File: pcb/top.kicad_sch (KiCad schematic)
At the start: 76 parts, among them J1 Conn_01x01, J10 Conn_01x01, J11 Conn_01x01, J2 Conn_01x01, J3 Conn_01x06, J4 Conn_01x01, J5 Conn_01x01, J6 Conn_01x01, J7 Conn_01x01, J8 Conn_01x01, J9 Conn_01x01, Q1 2N7002, Q2 2N7002, Q3 2N7002, Q4 2N7002, U1 L78L05_SOT89, U2 PIC12F629-ISN, U3 L78L08_SO8

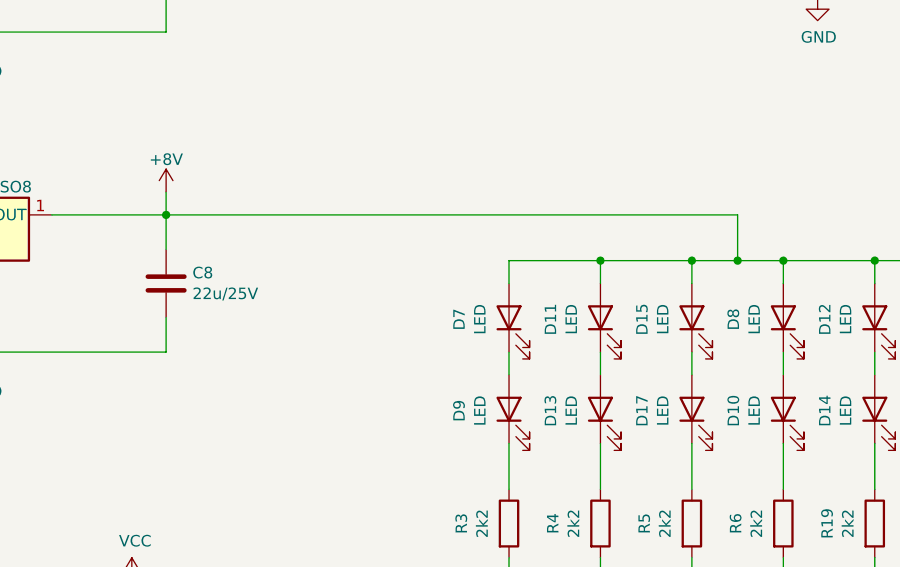
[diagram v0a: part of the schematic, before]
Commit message: Add optinal tantalum capacitor.
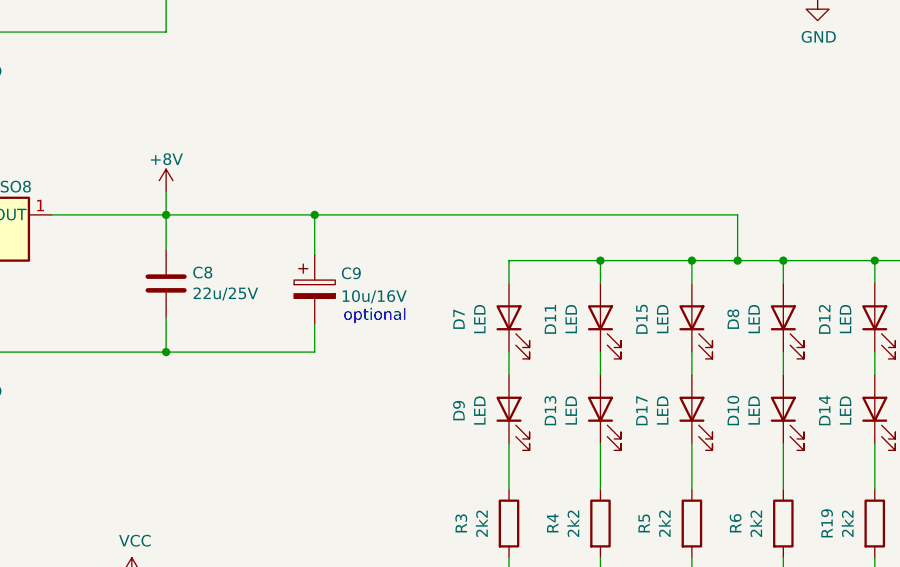
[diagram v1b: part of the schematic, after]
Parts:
- added C9: 10u/16V, Capacitor_Tantalum_SMD:CP_EIA-3216-10_Kemet-I, symbol Device:C_Polarized
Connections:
- net +8V: now also C9.1
- net GND: now also C9.2
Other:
- note added: "optional"
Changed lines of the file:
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@@
   (title_block
     (title "Osvětlení vozů Balm MTB model - horní deska")
-    (date "2021-12-23")
-    (rev "2.0")
+    (date "2023-03-18")
+    (rev "2.1")
     (company "Model Railroader Club Brno I – KMŽ Brno I – https://kmz-brno.cz/")
     (comment 1 "Jan Horáček; inspirováno https://usuaris.tinet.cat/fmco/dccfunc_en.html")
@@
   (junction (at 115.57 52.07) (diameter 0) (color 0 0 0 0)
   )
+  (junction (at 156.21 87.63) (diameter 0) (color 0 0 0 0)
+  )
   (junction (at 234.95 116.84) (diameter 0) (color 0 0 0 0)
   )
@@
   )
   (junction (at 83.82 44.45) (diameter 0) (color 0 0 0 0)
+  )
+  (junction (at 172.72 72.39) (diameter 0) (color 0 0 0 0)
   )
   (junction (at 92.71 36.83) (diameter 0) (color 0 0 0 0)
@@
     (stroke (width 0) (type default) (color 0 0 0 0))
   )
-  (wire (pts (xy 156.21 72.39) (xy 219.71 72.39))
+  (wire (pts (xy 172.72 72.39) (xy 219.71 72.39))
+    (stroke (width 0) (type default) (color 0 0 0 0))
+  )
+  (wire (pts (xy 156.21 72.39) (xy 172.72 72.39))
     (stroke (width 0) (type default) (color 0 0 0 0))
   )
@@
     (stroke (width 0) (type default) (color 0 0 0 0))
   )
+  (wire (pts (xy 172.72 84.455) (xy 172.72 87.63))
+    (stroke (width 0) (type default) (color 0 0 0 0))
+  )
   (wire (pts (xy 135.89 87.63) (xy 156.21 87.63))
     (stroke (width 0) (type default) (color 0 0 0 0))
@@
     (stroke (width 0) (type default) (color 0 0 0 0))
   )
+  (wire (pts (xy 172.72 87.63) (xy 156.21 87.63))
+    (stroke (width 0) (type default) (color 0 0 0 0))
+  )
   (wire (pts (xy 100.33 146.05) (xy 100.33 148.59))
     (stroke (width 0) (type default) (color 0 0 0 0))
@@
   )
   (wire (pts (xy 95.25 118.11) (xy 100.33 118.11))
+    (stroke (width 0) (type default) (color 0 0 0 0))
+  )
+  (wire (pts (xy 172.72 72.39) (xy 172.72 76.835))
     (stroke (width 0) (type default) (color 0 0 0 0))
   )
@@
   )
   (text "Programming\nconnector" (at 233.68 29.21 0)
+    (effects (font (size 1.27 1.27)) (justify left bottom))
+  )
+  (text "optional" (at 175.895 84.455 0)
     (effects (font (size 1.27 1.27)) (justify left bottom))
   )
@@
     (pin "1")
   )
+  (symbol (lib_id "Device:C_Polarized") (at 172.72 80.645 0) (unit 1)
+    (in_bom yes) (on_board yes) (fields_autoplaced)
+    (property "Reference" "C9" (id 0) (at 175.641 78.9213 0)
+      (effects (font (size 1.27 1.27)) (justify left))
+    )
+    (property "Value" "10u/16V" (id 1) (at 175.641 81.4582 0)
+      (effects (font (size 1.27 1.27)) (justify left))
+    )
+    (property "Footprint" "Capacitor_Tantalum_SMD:CP_EIA-3216-10_Kemet-I" (id 2) (at 173.6852 84.455 0)
+      (effects (font (size 1.27 1.27)) hide)
+    )
+    (property "Datasheet" "~" (id 3) (at 172.72 80.645 0)
+      (effects (font (size 1.27 1.27)) hide)
+    )
+    (pin "1")
+    (pin "2")
+  )
   (symbol (lib_id "Mechanical:MountingHole") (at 76.2 181.61 0) (unit 1)
     (in_bom yes) (on_board yes)
@@
       (reference "C8") (unit 1) (value "22u/25V") (footprint "Capacitor_SMD:C_0805_2012Metric_Pad1.18x1.45mm_HandSolder")
     )
+    (path "/802d2433-37f7-42c0-af96-9720c4dded53"
+      (reference "C9") (unit 1) (value "10u/16V") (footprint "Capacitor_Tantalum_SMD:CP_EIA-3216-10_Kemet-I")
+    )
     (path "/00000000-0000-0000-0000-000061c6e829"

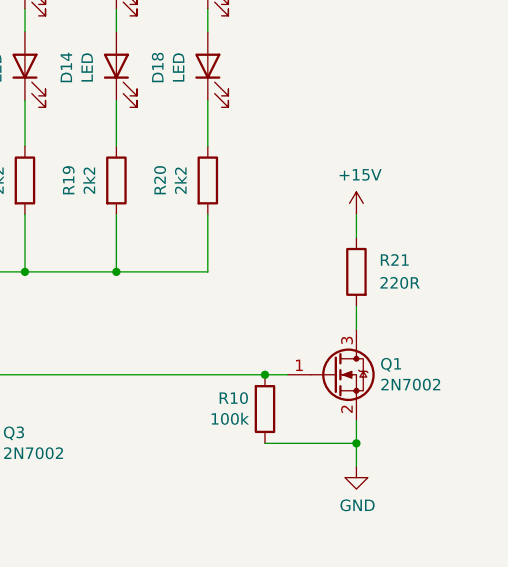
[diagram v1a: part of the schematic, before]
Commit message: Add JLCPCB_IGNORE or LCSC number.
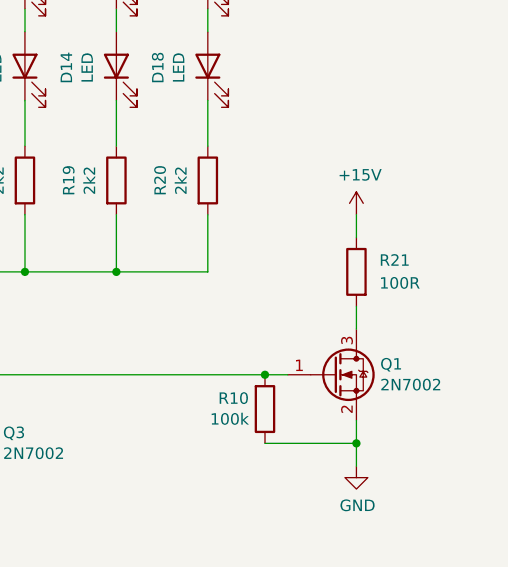
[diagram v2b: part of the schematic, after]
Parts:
- C3, C5, C9, D10, D11, D12, D13, D14, D15, D16, D17, D18, D7, D8, D9, H1, H10, H2, H3, H4, H5, H6, H7, H8, H9, J1, J10, J11, J2, J3, J4, J5, J6, J7, J8, J9, L1, R1: JLCPCB_IGNORE (none) -> true
- R21: value 220R -> 100R; JLCPCB_IGNORE (none) -> true
- U2: LCSC (none) -> C8226
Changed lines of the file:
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@@
+      (effects (font (size 1.27 1.27)) hide)
+    )
+    (property "JLCPCB_IGNORE" "true" (id 4) (at 35.56 29.21 0)
       (effects (font (size 1.27 1.27)) hide)
     )
@@
       (effects (font (size 1.27 1.27)) hide)
     )
+    (property "JLCPCB_IGNORE" "true" (id 4) (at 35.56 55.88 0)
+      (effects (font (size 1.27 1.27)) hide)
+    )
     (pin "1")
   )
@@
     )
     (property "Datasheet" "http://ww1.microchip.com/downloads/en/DeviceDoc/41190G.pdf" (id 3) (at 152.4 135.89 0)
+      (effects (font (size 1.27 1.27)) hide)
+    )
+    (property "LCSC" "C8226" (id 4) (at 152.4 135.89 0)
       (effects (font (size 1.27 1.27)) hide)
     )
@@
       (effects (font (size 1.27 1.27)) hide)
     )
+    (property "JLCPCB_IGNORE" "true" (id 4) (at 236.22 38.1 0)
+      (effects (font (size 1.27 1.27)) hide)
+    )
     (pin "1")
     (pin "2")
@@
       (effects (font (size 1.27 1.27)) hide)
     )
+    (property "JLCPCB_IGNORE" "true" (id 4) (at 194.31 83.82 0)
+      (effects (font (size 1.27 1.27)) hide)
+    )
     (pin "1")
     (pin "2")
@@
       (effects (font (size 1.27 1.27)) hide)
     )
+    (property "JLCPCB_IGNORE" "true" (id 4) (at 204.47 83.82 0)
+      (effects (font (size 1.27 1.27)) hide)
+    )
     (pin "1")
     (pin "2")
@@
       (effects (font (size 1.27 1.27)) hide)
     )
+    (property "JLCPCB_IGNORE" "true" (id 4) (at 214.63 83.82 0)
+      (effects (font (size 1.27 1.27)) hide)
+    )
     (pin "1")
     (pin "2")
@@
       (effects (font (size 1.27 1.27)) hide)
     )
+    (property "JLCPCB_IGNORE" "true" (id 4) (at 224.79 83.82 0)
+      (effects (font (size 1.27 1.27)) hide)
+    )
     (pin "1")
     (pin "2")
@@
       (effects (font (size 1.27 1.27)) hide)
     )
+    (property "JLCPCB_IGNORE" "true" (id 4) (at 234.95 83.82 0)
+      (effects (font (size 1.27 1.27)) hide)
+    )
     (pin "1")
     (pin "2")
@@
       (effects (font (size 1.27 1.27)) hide)
     )
+    (property "JLCPCB_IGNORE" "true" (id 4) (at 245.11 83.82 0)
+      (effects (font (size 1.27 1.27)) hide)
+    )
     (pin "1")
     (pin "2")
@@
       (effects (font (size 1.27 1.27)) hide)
     )
+    (property "JLCPCB_IGNORE" "true" (id 4) (at 194.31 93.98 0)
+      (effects (font (size 1.27 1.27)) hide)
+    )
     (pin "1")
     (pin "2")
@@
       (effects (font (size 1.27 1.27)) hide)
     )
+    (property "JLCPCB_IGNORE" "true" (id 4) (at 204.47 93.98 0)
+      (effects (font (size 1.27 1.27)) hide)
+    )
     (pin "1")
     (pin "2")
@@
       (effects (font (size 1.27 1.27)) hide)
     )
+    (property "JLCPCB_IGNORE" "true" (id 4) (at 214.63 93.98 0)
+      (effects (font (size 1.27 1.27)) hide)
+    )
     (pin "1")
     (pin "2")
@@
       (effects (font (size 1.27 1.27)) hide)
     )
+    (property "JLCPCB_IGNORE" "true" (id 4) (at 224.79 93.98 0)
+      (effects (font (size 1.27 1.27)) hide)
+    )
     (pin "1")
     (pin "2")
@@
       (effects (font (size 1.27 1.27)) hide)
     )
+    (property "JLCPCB_IGNORE" "true" (id 4) (at 234.95 93.98 0)
+      (effects (font (size 1.27 1.27)) hide)
+    )
     (pin "1")
     (pin "2")
@@
       (effects (font (size 1.27 1.27)) hide)
     )
+    (property "JLCPCB_IGNORE" "true" (id 4) (at 245.11 93.98 0)
+      (effects (font (size 1.27 1.27)) hide)
+    )
     (pin "1")
     (pin "2")
@@
       (effects (font (size 1.27 1.27)) hide)
     )
+    (property "JLCPCB_IGNORE" "true" (id 4) (at 31.75 166.37 0)
+      (effects (font (size 1.27 1.27)) hide)
+    )
   )
   (symbol (lib_id "Mechanical:MountingHole") (at 31.75 171.45 0) (unit 1)
@@
       (effects (font (size 1.27 1.27)) hide)
     )
+    (property "JLCPCB_IGNORE" "true" (id 4) (at 31.75 171.45 0)
+      (effects (font (size 1.27 1.27)) hide)
+    )
   )
   (symbol (lib_id "Mechanical:MountingHole") (at 31.75 176.53 0) (unit 1)
@@
       (effects (font (size 1.27 1.27)) hide)
     )
+    (property "JLCPCB_IGNORE" "true" (id 4) (at 31.75 176.53 0)
+      (effects (font (size 1.27 1.27)) hide)
+    )
   )
   (symbol (lib_id "Mechanical:MountingHole") (at 31.75 181.61 0) (unit 1)
@@
     )
     (property "Datasheet" "~" (id 3) (at 31.75 181.61 0)
+      (effects (font (size 1.27 1.27)) hide)
+    )
+    (property "JLCPCB_IGNORE" "true" (id 4) (at 31.75 181.61 0)
       (effects (font (size 1.27 1.27)) hide)
     )
@@
       (effects (font (size 1.27 1.27)) hide)
     )
+    (property "JLCPCB_IGNORE" "true" (id 4) (at 35.56 59.69 0)
+      (effects (font (size 1.27 1.27)) hide)
+    )
     (pin "1")
   )
@@
       (effects (font (size 1.27 1.27)) hide)
     )
+    (property "JLCPCB_IGNORE" "true" (id 4) (at 35.56 33.02 0)
+      (effects (font (size 1.27 1.27)) hide)
+    )
     (pin "1")
   )
@@
     )
     (property "Datasheet" "~" (id 3) (at 30.48 80.01 0)
+      (effects (font (size 1.27 1.27)) hide)
+    )
+    (property "JLCPCB_IGNORE" "true" (id 4) (at 30.48 80.01 0)
       (effects (font (size 1.27 1.27)) hide)
     )
@@
       (effects (font (size 1.27 1.27)) hide)
     )
+    (property "JLCPCB_IGNORE" "true" (id 4) (at 58.42 115.57 0)
+      (effects (font (size 1.27 1.27)) hide)
+    )
     (pin "1")
   )
@@
       (effects (font (size 1.27 1.27)) hide)
     )
+    (property "JLCPCB_IGNORE" "true" (id 4) (at 58.42 118.11 0)
+      (effects (font (size 1.27 1.27)) hide)
+    )
     (pin "1")
   )
@@
       (effects (font (size 1.27 1.27)) hide)
     )
+    (property "JLCPCB_IGNORE" "true" (id 4) (at 90.17 115.57 0)
+      (effects (font (size 1.27 1.27)) hide)
+    )
     (pin "1")
   )
@@
       (effects (font (size 1.27 1.27)) hide)
     )
+    (property "JLCPCB_IGNORE" "true" (id 4) (at 90.17 118.11 0)
+      (effects (font (size 1.27 1.27)) hide)
+    )
     (pin "1")
   )
@@
       (effects (font (size 1.27 1.27)) hide)
     )
+    (property "JLCPCB_IGNORE" "true" (id 4) (at 35.56 36.83 0)
+      (effects (font (size 1.27 1.27)) hide)
+    )
     (pin "1")
   )
@@
       (effects (font (size 1.27 1.27)) hide)
     )
+    (property "JLCPCB_IGNORE" "true" (id 4) (at 35.56 63.5 0)
+      (effects (font (size 1.27 1.27)) hide)
+    )
     (pin "1")
   )
@@
     )
     (property "Datasheet" "~" (id 3) (at 48.26 80.01 0)
+      (effects (font (size 1.27 1.27)) hide)
+    )
+    (property "JLCPCB_IGNORE" "true" (id 4) (at 48.26 80.01 0)
       (effects (font (size 1.27 1.27)) hide)
     )
@@
       (effects (font (size 1.27 1.27)) hide)
     )
+    (property "JLCPCB_IGNORE" "true" (id 5) (at 67.31 81.28 0)
+      (effects (font (size 1.27 1.27)) hide)
+    )
     (pin "1")
     (pin "2")
@@
       (effects (font (size 1.27 1.27)) hide)
     )
+    (property "JLCPCB_IGNORE" "true" (id 4) (at 67.31 87.63 0)
+      (effects (font (size 1.27 1.27)) hide)
+    )
     (pin "1")
     (pin "2")
@@
       (effects (font (size 1.27 1.27)) hide)
     )
+    (property "JLCPCB_IGNORE" "true" (id 4) (at 54.61 171.45 0)
+      (effects (font (size 1.27 1.27)) hide)
+    )
   )
   (symbol (lib_id "Mechanical:MountingHole") (at 54.61 166.37 0) (unit 1)
@@
     )
     (property "Datasheet" "~" (id 3) (at 54.61 166.37 0)
+      (effects (font (size 1.27 1.27)) hide)
+    )
+    (property "JLCPCB_IGNORE" "true" (id 4) (at 54.61 166.37 0)
       (effects (font (size 1.27 1.27)) hide)
     )
@@
       (effects (font (size 1.27 1.27)) hide)
     )
+    (property "JLCPCB_IGNORE" "true" (id 4) (at 76.2 176.53 0)
+      (effects (font (size 1.27 1.27)) hide)
+    )
   )
   (symbol (lib_id "Device:R") (at 261.62 116.84 0) (mirror y) (unit 1)
@@
       (effects (font (size 1.27 1.27)) (justify right))
     )
-    (property "Value" "220R" (id 1) (at 264.16 118.11 0)
+    (property "Value" "100R" (id 1) (at 264.16 118.11 0)
       (effects (font (size 1.27 1.27)) (justify right))
     )
@@
     )
     (property "LCSC" "" (id 4) (at 261.62 116.84 0)
+      (effects (font (size 1.27 1.27)) hide)
+    )
+    (property "JLCPCB_IGNORE" "true" (id 5) (at 261.62 116.84 0)
       (effects (font (size 1.27 1.27)) hide)
     )
@@
       (effects (font (size 1.27 1.27)) hide)
     )
+    (property "JLCPCB_IGNORE" "true" (id 4) (at 172.72 80.645 0)
+      (effects (font (size 1.27 1.27)) hide)
+    )
     (pin "1")
     (pin "2")
@@
     )
     (property "Datasheet" "~" (id 3) (at 76.2 181.61 0)
+      (effects (font (size 1.27 1.27)) hide)
+    )
+    (property "JLCPCB_IGNORE" "true" (id 4) (at 76.2 181.61 0)
       (effects (font (size 1.27 1.27)) hide)
     )
@@
       (effects (font (size 1.27 1.27)) hide)
     )
+    (property "JLCPCB_IGNORE" "true" (id 4) (at 76.2 166.37 0)
+      (effects (font (size 1.27 1.27)) hide)
+    )
   )
   (symbol (lib_id "Device:C") (at 115.57 80.01 0) (unit 1)
@@
       (effects (font (size 1.27 1.27)) hide)
     )
+    (property "JLCPCB_IGNORE" "true" (id 4) (at 76.2 171.45 0)
+      (effects (font (size 1.27 1.27)) hide)
+    )
   )
   (symbol (lib_id "power:GND") (at 135.89 87.63 0) (unit 1)
@@
     )
     (path "/5ed39f78-a424-4fab-b48b-d1e85e43d60d"
-      (reference "R21") (unit 1) (value "220R") (footprint "Resistor_SMD:R_2512_6332Metric_Pad1.40x3.35mm_HandSolder")
+      (reference "R21") (unit 1) (value "100R") (footprint "Resistor_SMD:R_2512_6332Metric_Pad1.40x3.35mm_HandSolder")
     )
     (path "/00000000-0000-0000-0000-000061c4dc59"
